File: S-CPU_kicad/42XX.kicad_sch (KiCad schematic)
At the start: 156 parts, among them U34 OR_2, U35 OR_2, U36 OR_2, U37 OR_2, U6 MUX

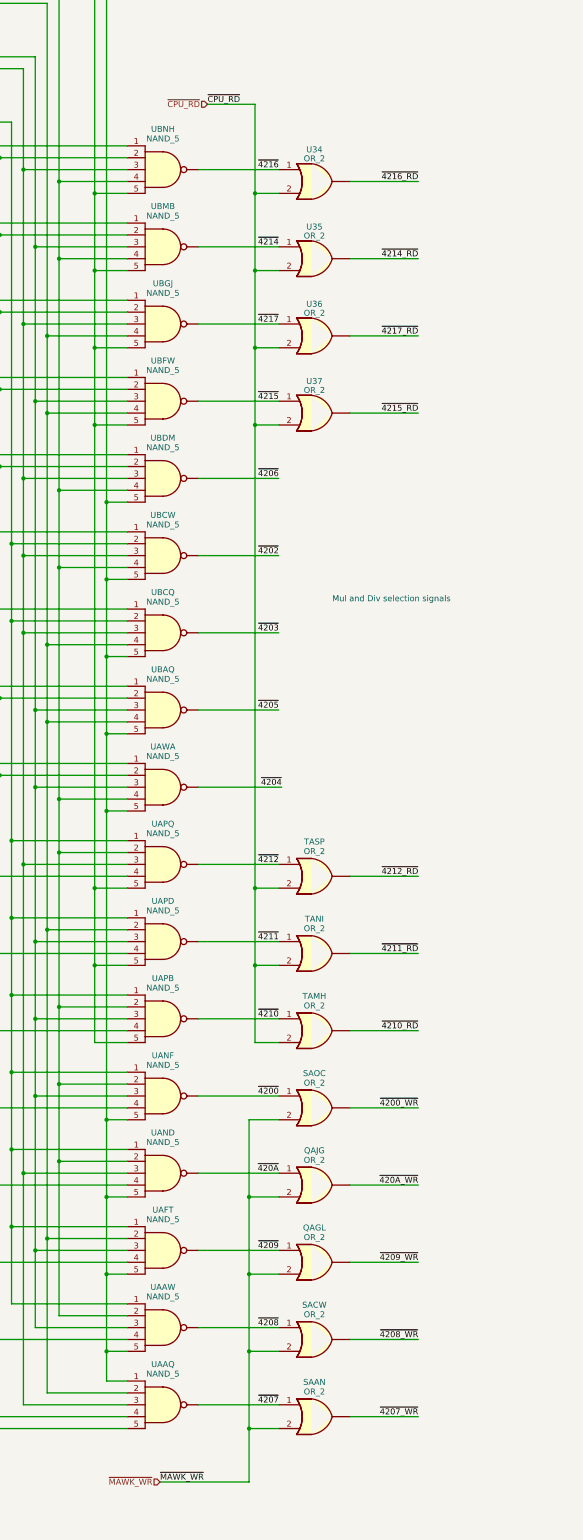
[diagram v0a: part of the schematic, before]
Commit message: Fixed complex gate names. Most fo the cells in the mul div section have been idnetified in SVG file.
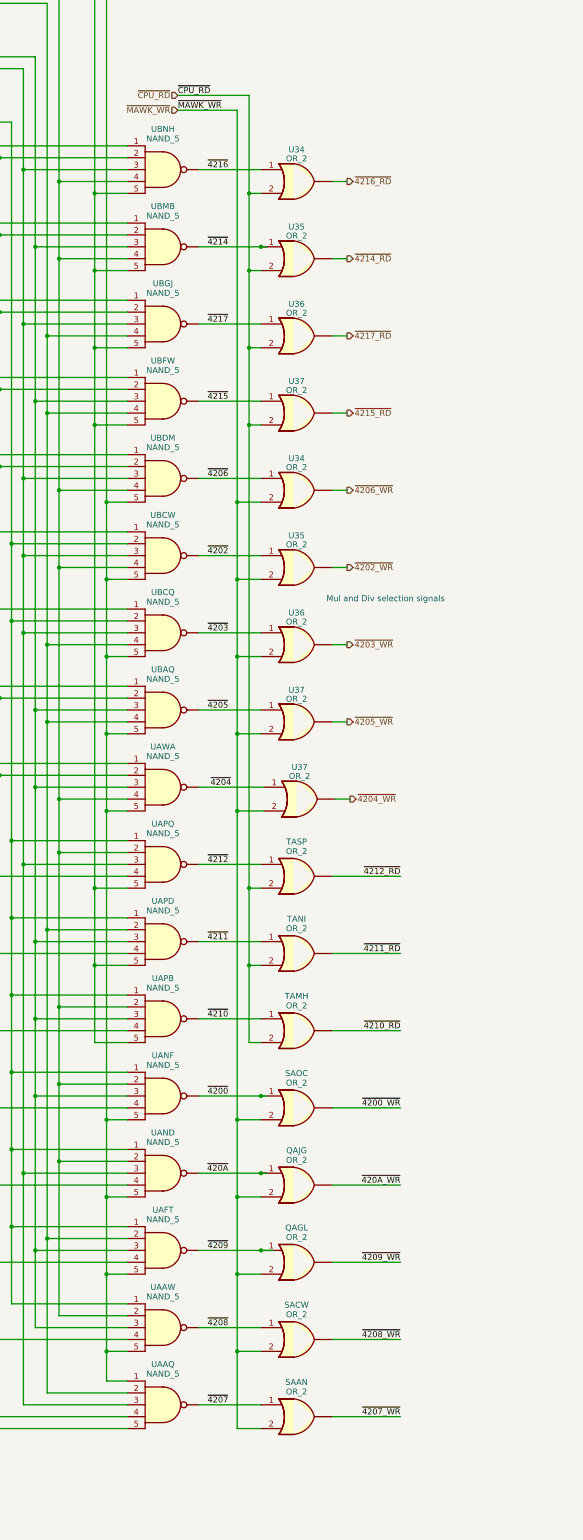
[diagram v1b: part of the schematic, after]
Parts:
- added U34, U35, U36, U37 (x2): OR_2, symbol Ricoh_Cells:OR_2
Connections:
- net ~{4202}: now also U35.1
- net ~{4203}: now also U36.1
- net ~{4204}: now also U37.1
- net ~{4205}: now also U37.1
- net ~{4206}: now also U34.1
- net ~{MAWK_WR}: now also U34.2, U35.2, U36.2, U37.2, U37.2
- new net ~{4202_WR}: U35.3
- new net ~{4203_WR}: U36.3
- new net ~{4204_WR}: U37.3
- new net ~{4205_WR}: U37.3
- new net ~{4206_WR}: U34.3
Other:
- moved on the sheet: QAGL, QAJG, SAAN, SACW, SAOC, TAMH, TANI, TASP, U34, U35, U36, U37

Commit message: Latch cell identified. Progress in Mul Div section.
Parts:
- removed U35: OR_2, symbol Ricoh_Cells:OR_2
- added HFWL: NOR_2, symbol Ricoh_Cells:NOR_2
- renumbered PBH0 to PBHO
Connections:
- net ~{4202}: now also HFWL.1
- net ~{MAWK_WR}: now also HFWL.2
- new net 4202_WR: HFWL.3

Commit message: MUL DIV section almost done.
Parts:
- removed U37 (x2): OR_2, symbol Ricoh_Cells:OR_2
- added HFWL (x2): NOR_2, symbol Ricoh_Cells:NOR_2
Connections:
- net ~{4204}: now also HFWL.1
- net ~{4205}: now also HFWL.1
- net ~{MAWK_WR}: now also HFWL.2, HFWL.2
- new net 4204_WR: HFWL.3
- new net 4205_WR: HFWL.3
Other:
- note added: "Mul and Div RW register signals"
- note removed: "Mul and Div selection signals"
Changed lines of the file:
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@@
     (stroke (width 0) (type default))
   )
+  (polyline (pts (xy 193.675 230.505) (xy 208.28 230.505))
+    (stroke (width 0) (type dash))
+  )
   (wire (pts (xy 481.33 398.78) (xy 481.33 224.155))
     (stroke (width 0) (type default))
@@
     (stroke (width 0) (type default))
   )
+  (polyline (pts (xy 199.39 373.38) (xy 208.28 373.38))
+    (stroke (width 0) (type dash))
+  )
   (wire (pts (xy 435.61 487.045) (xy 485.14 487.045))
     (stroke (width 0) (type default))
@@
     (stroke (width 0) (type default))
   )
+  (polyline (pts (xy 208.28 230.505) (xy 208.28 373.38))
+    (stroke (width 0) (type dash))
+  )
   (wire (pts (xy 147.32 283.21) (xy 127.635 283.21))
     (stroke (width 0) (type default))
@@
     (effects (font (size 5 5) (thickness 1) bold) (justify left bottom))
   )
-  (text "Mul and Div selection signals" (at 189.865 326.39 0)
-    (effects (font (size 1.27 1.27)) (justify left bottom))
+  (text "Mul and Div RW\nregister signals" (at 212.09 299.085 0)
+    (effects (font (size 2 2)) (justify left bottom))
   )
   (text "H counter is reset and V counter is incremented\non HBLANK falling egde"
@@
     (effects (font (size 1.27 1.27)) (justify left))
   )
-  (hierarchical_label "~{4205_WR}" (shape output) (at 194.31 351.79 0) (fields_autoplaced)
+  (hierarchical_label "4205_WR" (shape output) (at 194.31 351.79 0) (fields_autoplaced)
     (effects (font (size 1.27 1.27)) (justify left))
   )
@@
     (effects (font (size 1.27 1.27)) (justify right))
   )
-  (hierarchical_label "~{4204_WR}" (shape output) (at 194.945 368.3 0) (fields_autoplaced)
+  (hierarchical_label "4204_WR" (shape output) (at 194.945 368.3 0) (fields_autoplaced)
     (effects (font (size 1.27 1.27)) (justify left))
   )
@@
     )
   )
+  (symbol (lib_id "Ricoh_Cells:NOR_2") (at 184.15 368.3 0) (unit 1)
+    (in_bom yes) (on_board yes) (dnp no) (fields_autoplaced)
+    (property "Reference" "HFWL" (at 184.1498 360.91 0)
+      (effects (font (size 1.27 1.27)))
+    )
+    (property "Value" "NOR_2" (at 184.1498 362.958 0)
+      (effects (font (size 1.27 1.27)))
+    )
+    (property "Footprint" "" (at 183.896 368.3 0)
+      (effects (font (size 1.27 1.27)) hide)
+    )
+    (property "Datasheet" "http://iceboy.a-singer.de/doc/dmg_cells.html#nor2" (at 184.15 375.92 0)
+      (effects (font (size 1.27 1.27)) hide)
+    )
+    (pin "1")
+    (pin "2")
+    (pin "3")
+    (instances
+      (project "S-CPU"
+        (path "/ca9d3ca9-0297-4b98-a109-b7c162ccc5c3/e7c40e34-ed5c-4acf-abcb-e687ca829050"
+          (reference "HFWL") (unit 1)
+        )
+        (path "/ca9d3ca9-0297-4b98-a109-b7c162ccc5c3/4dc5cd9a-499d-4e55-930f-d6021c4e63f2"
+          (reference "MFAE") (unit 1)
+        )
+      )
+    )
+  )
   (symbol (lib_id "Ricoh_Cells:DFFSR") (at 416.56 163.195 0) (unit 1)
     (in_bom yes) (on_board yes) (dnp no) (fields_autoplaced)
@@
     )
   )
+  (symbol (lib_id "Ricoh_Cells:NOR_2") (at 183.515 351.79 0) (unit 1)
+    (in_bom yes) (on_board yes) (dnp no) (fields_autoplaced)
+    (property "Reference" "HFWL" (at 183.5148 344.4 0)
+      (effects (font (size 1.27 1.27)))
+    )
+    (property "Value" "NOR_2" (at 183.5148 346.448 0)
+      (effects (font (size 1.27 1.27)))
+    )
+    (property "Footprint" "" (at 183.261 351.79 0)
+      (effects (font (size 1.27 1.27)) hide)
+    )
+    (property "Datasheet" "http://iceboy.a-singer.de/doc/dmg_cells.html#nor2" (at 183.515 359.41 0)
+      (effects (font (size 1.27 1.27)) hide)
+    )
+    (pin "1")
+    (pin "2")
+    (pin "3")
+    (instances
+      (project "S-CPU"
+        (path "/ca9d3ca9-0297-4b98-a109-b7c162ccc5c3/e7c40e34-ed5c-4acf-abcb-e687ca829050"
+          (reference "HFWL") (unit 1)
+        )
+        (path "/ca9d3ca9-0297-4b98-a109-b7c162ccc5c3/4dc5cd9a-499d-4e55-930f-d6021c4e63f2"
+          (reference "NFBB") (unit 1)
+        )
+      )
+    )
+  )
   (symbol (lib_id "Ricoh_Cells:XOR") (at 685.165 426.72 0) (unit 1)
     (in_bom yes) (on_board yes) (dnp no) (fields_autoplaced)
@@
     )
   )
-  (symbol (lib_id "Ricoh_Cells:OR_2") (at 183.515 351.79 0) (unit 1)
-    (in_bom yes) (on_board yes) (dnp no) (fields_autoplaced)
-    (property "Reference" "U37" (at 183.5148 344.9701 0)
-      (effects (font (size 1.27 1.27)))
-    )
-    (property "Value" "OR_2" (at 183.5148 346.8911 0)
-      (effects (font (size 1.27 1.27)))
-    )
-    (property "Footprint" "" (at 183.261 351.79 0)
-      (effects (font (size 1.27 1.27)) hide)
-    )
-    (property "Datasheet" "http://iceboy.a-singer.de/doc/dmg_cells.html#or2" (at 183.515 359.41 0)
-      (effects (font (size 1.27 1.27)) hide)
-    )
-    (pin "1")
-    (pin "2")
-    (pin "3")
-    (instances
-      (project "S-CPU"
-        (path "/ca9d3ca9-0297-4b98-a109-b7c162ccc5c3/c42cdb83-bc69-486b-820b-017180bd7612"
-          (reference "U37") (unit 1)
-        )
-        (path "/ca9d3ca9-0297-4b98-a109-b7c162ccc5c3/4dc5cd9a-499d-4e55-930f-d6021c4e63f2"
-          (reference "U4") (unit 1)
-        )
-      )
-    )
-  )
   (symbol (lib_id "Ricoh_Cells:NAND_2") (at 349.25 151.765 0) (unit 1)
     (in_bom yes) (on_board yes) (dnp no) (fields_autoplaced)
@@
         )
       )
-    )
-  )
-  (symbol (lib_id "Ricoh_Cells:OR_2") (at 184.15 368.3 0) (unit 1)
-    (in_bom yes) (on_board yes) (dnp no) (fields_autoplaced)
-    (property "Reference" "U37" (at 184.1498 361.4801 0)
-      (effects (font (size 1.27 1.27)))
-    )
-    (property "Value" "OR_2" (at 184.1498 363.4011 0)
-      (effects (font (size 1.27 1.27)))
-    )
-    (property "Footprint" "" (at 183.896 368.3 0)
-      (effects (font (size 1.27 1.27)) hide)
-    )
-    (property "Datasheet" "http://iceboy.a-singer.de/doc/dmg_cells.html#or2" (at 184.15 375.92 0)
-      (effects (font (size 1.27 1.27)) hide)
-    )
-    (pin "1")
-    (pin "2")
-    (pin "3")
-    (instances
-      (project "S-CPU"
-        (path "/ca9d3ca9-0297-4b98-a109-b7c162ccc5c3/c42cdb83-bc69-486b-820b-017180bd7612"
-          (reference "U37") (unit 1)
-        )
-        (path "/ca9d3ca9-0297-4b98-a109-b7c162ccc5c3/4dc5cd9a-499d-4e55-930f-d6021c4e63f2"
-          (reference "U5") (unit 1)
-        )
-      )

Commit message: More MUL DIV section updates,
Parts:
- ABVA1: symbol Ricoh_Cells:TRI_BUF_IF1 -> Ricoh_Cells:TRI_BUF_IF0
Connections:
- net at SAMW.2: now also PBHO.1; no longer PBHO.2
- net at SAMW.2: now also PBHO.2; no longer PBHO.1
- net VBLANK_NMI: no longer names the net of PAEB.1, SALQ.3
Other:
- moved on the sheet: ABWF1, ABXH1, JP2I0, PBHO, TAVF

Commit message: ADDR and DAT bus progress
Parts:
- ABVA1: value TRI_BUF_IF0 -> TRI_BUF_IF1; symbol Ricoh_Cells:TRI_BUF_IF0 -> Ricoh_Cells:TRI_BUF_IF1
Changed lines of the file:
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@@
       (effects (font (size 1.27 1.27)) hide)
     )
-    (property "Datasheet" "http://iceboy.a-singer.de/doc/dmg_cells.html#ibuf" (at 702.31 193.04 0)
+    (property "Datasheet" "" (at 702.31 193.04 0)
       (effects (font (size 1.27 1.27)) hide)
     )
@@
       (effects (font (size 1.27 1.27)) hide)
     )
-    (property "Datasheet" "http://iceboy.a-singer.de/doc/dmg_cells.html#tri_buf_if0" (at 455.93 119.38 0)
+    (property "Datasheet" "http://iceboy.a-singer.de/doc/dmg_cells.html#tri_inv_if0" (at 455.93 119.38 0)
       (effects (font (size 1.27 1.27)) hide)
     )
@@
       (effects (font (size 1.27 1.27)) hide)
     )
-    (property "Datasheet" "http://iceboy.a-singer.de/doc/dmg_cells.html#tri_buf_if0" (at 350.52 87.63 0)
+    (property "Datasheet" "http://iceboy.a-singer.de/doc/dmg_cells.html#tri_inv_if0" (at 350.52 87.63 0)
       (effects (font (size 1.27 1.27)) hide)
     )
@@
       (effects (font (size 1.27 1.27)) hide)
     )
-    (property "Datasheet" "http://iceboy.a-singer.de/doc/dmg_cells.html#ibuf" (at 288.29 86.36 0)
+    (property "Datasheet" "" (at 288.29 86.36 0)
       (effects (font (size 1.27 1.27)) hide)
     )
@@
       (effects (font (size 1.27 1.27)) hide)
     )
-    (property "Datasheet" "http://iceboy.a-singer.de/doc/dmg_cells.html#tri_buf_if0" (at 455.93 83.82 0)
+    (property "Datasheet" "http://iceboy.a-singer.de/doc/dmg_cells.html#tri_inv_if0" (at 455.93 83.82 0)
       (effects (font (size 1.27 1.27)) hide)
     )
@@
       (effects (font (size 1.27 1.27)) hide)
     )
-    (property "Datasheet" "http://iceboy.a-singer.de/doc/dmg_cells.html#tri_buf_if0" (at 350.52 105.41 0)
+    (property "Datasheet" "http://iceboy.a-singer.de/doc/dmg_cells.html#tri_inv_if0" (at 350.52 105.41 0)
       (effects (font (size 1.27 1.27)) hide)
     )
@@
       (effects (font (size 1.27 1.27)) hide)
     )
-    (property "Datasheet" "http://iceboy.a-singer.de/doc/dmg_cells.html#tri_buf_if0" (at 455.93 137.16 0)
+    (property "Datasheet" "http://iceboy.a-singer.de/doc/dmg_cells.html#tri_inv_if0" (at 455.93 137.16 0)
       (effects (font (size 1.27 1.27)) hide)
     )
@@
       (effects (font (size 1.27 1.27)) hide)
     )
-    (property "Datasheet" "http://iceboy.a-singer.de/doc/dmg_cells.html#tri_buf_if0" (at 455.93 101.6 0)
+    (property "Datasheet" "http://iceboy.a-singer.de/doc/dmg_cells.html#tri_inv_if0" (at 455.93 101.6 0)
       (effects (font (size 1.27 1.27)) hide)
     )
@@
       (effects (font (size 1.27 1.27)) hide)
     )
-    (property "Datasheet" "http://iceboy.a-singer.de/doc/dmg_cells.html#ibuf" (at 469.9 203.835 0)
+    (property "Datasheet" "" (at 469.9 203.835 0)
       (effects (font (size 1.27 1.27)) hide)
     )
@@
       (effects (font (size 1.27 1.27)) hide)
     )
-    (property "Datasheet" "http://iceboy.a-singer.de/doc/dmg_cells.html#ibuf" (at 288.29 104.14 0)
+    (property "Datasheet" "" (at 288.29 104.14 0)
       (effects (font (size 1.27 1.27)) hide)
     )
@@
   (symbol (lib_id "Ricoh_Cells:XOR") (at 492.76 449.58 0) (unit 1)
     (in_bom yes) (on_board yes) (dnp no) (fields_autoplaced)
-    (property "Reference" "DCFC" (at 492.3915 442.7601 0)
+    (property "Reference" "DCFC" (at 492.3915 442.19 0)
       (effects (font (size 1.27 1.27)))
     )
-    (property "Value" "XOR" (at 492.3915 444.6811 0)
+    (property "Value" "XOR" (at 492.3915 444.238 0)
       (effects (font (size 1.27 1.27)))
     )
@@
         )
         (path "/ca9d3ca9-0297-4b98-a109-b7c162ccc5c3/4dc5cd9a-499d-4e55-930f-d6021c4e63f2"
-          (reference "DCFC") (unit 1)
+          (reference "DADP") (unit 1)
         )
       )
@@
       (effects (font (size 1.27 1.27)) hide)
     )
-    (property "Datasheet" "http://iceboy.a-singer.de/doc/dmg_cells.html#tri_buf_if0" (at 455.93 154.94 0)
+    (property "Datasheet" "http://iceboy.a-singer.de/doc/dmg_cells.html#tri_inv_if0" (at 455.93 154.94 0)
       (effects (font (size 1.27 1.27)) hide)
     )
@@
     )
   )
-  (symbol (lib_id "Ricoh_Cells:TRI_BUF_IF0") (at 349.25 59.69 0) (unit 1)
+  (symbol (lib_id "Ricoh_Cells:TRI_BUF_IF1") (at 349.25 59.69 0) (unit 1)
     (in_bom yes) (on_board yes) (dnp no) (fields_autoplaced)
     (property "Reference" "ABVA1" (at 349.25 65.032 0)
       (effects (font (size 1.27 1.27)))
     )
-    (property "Value" "TRI_BUF_IF0" (at 349.25 67.31 0)
+    (property "Value" "TRI_BUF_IF1" (at 349.25 67.31 0)
       (effects (font (size 1.27 1.27)))
     )

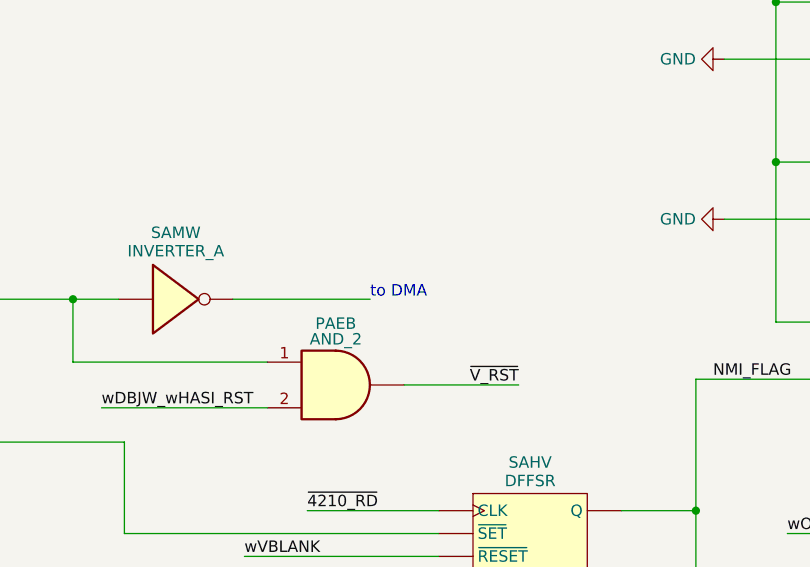
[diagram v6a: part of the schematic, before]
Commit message: DMA progress. Most gates identified.
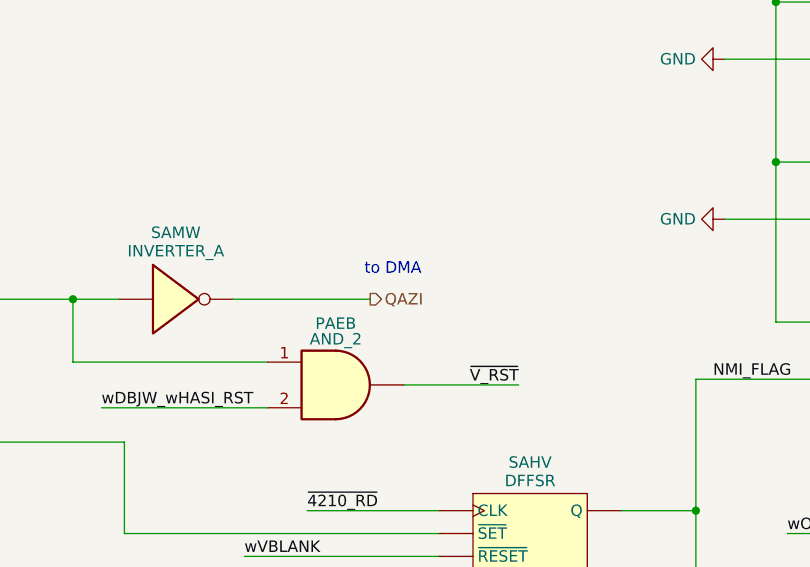
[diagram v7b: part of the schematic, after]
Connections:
- net QAZI: now reaches SAMW.2
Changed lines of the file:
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@@
     (effects (font (size 5 5) (thickness 1) bold) (justify left bottom))
   )
-  (text "to DMA" (at 398.78 135.89 0)
+  (text "to DMA" (at 398.145 133.35 0)
     (effects (font (size 1.27 1.27)) (justify left bottom))
   )
@@
     (effects (font (size 1.27 1.27)) (justify left))
   )
+  (hierarchical_label "QAZI" (shape output) (at 398.78 135.89 0) (fields_autoplaced)
+    (effects (font (size 1.27 1.27)) (justify left))
+  )
